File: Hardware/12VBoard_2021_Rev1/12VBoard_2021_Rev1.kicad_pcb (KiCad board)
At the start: 2 copper layers, 125 parts, among them Q1 2N7000, Q2 2N7000, Q3 NTR2101P, Q4 2N7000, Q5 2N7000, Q6 2N7000, Q7 2N7000, U1 LM2576SX-5.0/NOPB, U10 LM5116, U11 INA198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

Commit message: Worked on layout
Low current bucks grouped with their componets
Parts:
- C1, C3, C4, C43, C45, C47, C49, C5, C6: footprint Capacitor_THT:CP_Axial_L20.0mm_D10.0mm_P26.00mm_Horizontal -> Capacitor_THT:CP_Radial_D10.0mm_P5.00mm
- C15, C18, C22, C27, C30, C37, C40: footprint Capacitor_THT:CP_Axial_L20.0mm_D10.0mm_P26.00mm_Horizontal -> Capacitor_THT:CP_Radial_D6.3mm_P2.50mm
- Conn3: footprint MRDT_Connectors:Anderson_2_Horizontal_Stacked -> MRDT_Connectors:Anderson_2_Horizontal_Side_by_Side
- R1: value 1.2k -> 3.3k
- R2: value 1.2k -> 500
- moved TP2 256.2 mm to (192.5, 133.1)
- moved C5 254.8 mm to (197.1, 124.0), turned to 180 degrees
- moved D10 250.7 mm to (191.1, 139.4), turned to 180 degrees
- moved U4 247.7 mm to (142.2, 138.6), turned to 180 degrees
- moved C9 247.3 mm to (204.2, 134.2), turned to 90 degrees
- moved C6 245.1 mm to (168.7, 123.2), turned to 180 degrees
- moved U14 244.3 mm to (109.8, 136.1), turned to 180 degrees
- moved R7 243.6 mm to (163.0, 136.9), turned to 180 degrees
- moved D11 243.4 mm to (163.0, 138.7), turned to 180 degrees
- moved TP8 242.0 mm to (103.6, 130.6)
- moved R6 241.5 mm to (191.1, 137.4), turned to 180 degrees
- moved U6 240.7 mm to (170.4, 139.6), turned to 180 degrees
- moved U1 240.5 mm to (222.2, 140.7), turned to 180 degrees
- moved D6 240.4 mm to (202.1, 130.3)
- moved U5 239.4 mm to (198.9, 140.1), turned to 180 degrees
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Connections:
- D13 pad 1: Net-(D13-Pad1) -> AGNDPGND
- D13 pad 2: /High Current Outputs/Multimedia/Extra/12V10AExtra -> Net-(D13-Pad2)
- D14 pad 1: Net-(D14-Pad1) -> AGNDPGND
- D14 pad 2: /High Current Outputs/Multimedia/Extra/12V10AMultimedia -> Net-(D14-Pad2)
- D16 pad 1: Net-(D16-Pad1) -> AGNDPGND
- D16 pad 2: /High Current Outputs/AuxMount/12V10AAuxMount -> Net-(D16-Pad2)
- D18 pad 1: Net-(D18-Pad1) -> AGNDPGND
- D18 pad 2: /High Current Outputs/Gimbal/12V5AGimbal -> Net-(D18-Pad2)
- D2 pad 1: Net-(D2-Pad1) -> AGNDPGND
- D2 pad 2: /High Current Outputs/PackVoltage -> Net-(D2-Pad2)
- D22 pad 1: Net-(D22-Pad1) -> AGNDPGND
- D22 pad 2: /High Current Outputs/Multimedia/Extra/12V3AMultimediaExtraLogic -> Net-(D22-Pad2)
- D24 pad 1: Net-(D24-Pad1) -> AGNDPGND
- D24 pad 2: /High Current Outputs/Gimbal/12V3AGimbalLogic -> Net-(D24-Pad2)
- D26 pad 1: Net-(D26-Pad1) -> AGNDPGND
- D26 pad 2: /High Current Outputs/AuxMount/12V3AAuxMountLogic -> Net-(D26-Pad2)
- D3 pad 1: Net-(D3-Pad1) -> AGNDPGND
- D3 pad 2: /High Current Outputs/5V -> Net-(D3-Pad2)
- R1 pad 1: Net-(D2-Pad1) -> /High Current Outputs/PackVoltage
- R1 pad 2: AGNDPGND -> Net-(D2-Pad2)
- R2 pad 1: Net-(D3-Pad1) -> /High Current Outputs/5V
- R2 pad 2: AGNDPGND -> Net-(D3-Pad2)
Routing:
- net /High Current Outputs/PackVoltage: track 0.00 -> 6.46 mm
- net Net-(D2-Pad2): track 0.00 -> 4.32 mm
- added copper zone on B.Cu, net AGNDPGND
- added copper zone on F.Cu, net AGNDPGND

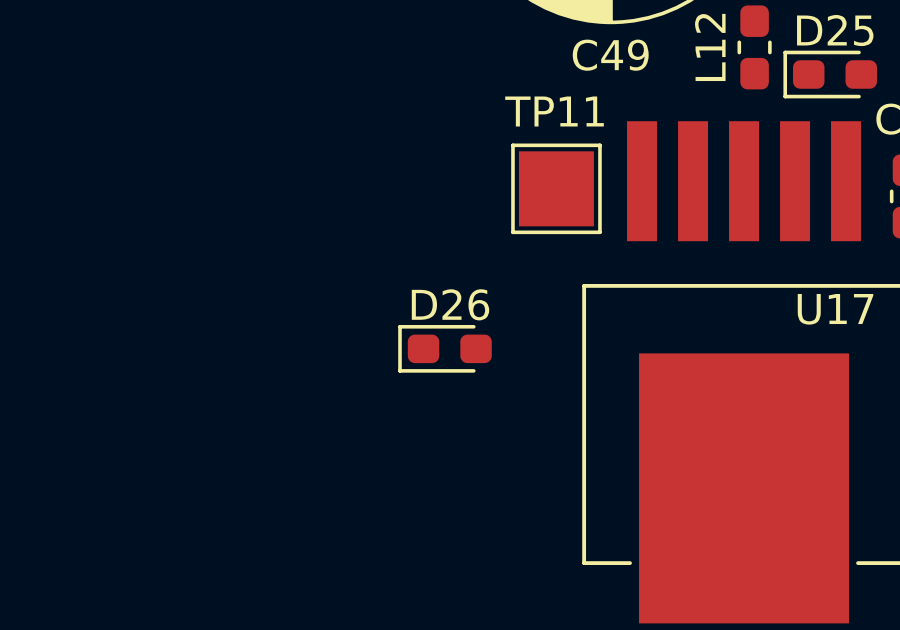
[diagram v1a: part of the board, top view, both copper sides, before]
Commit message: Missing footprints issue found
Library difference between computer caused footprints not to appear on the layout
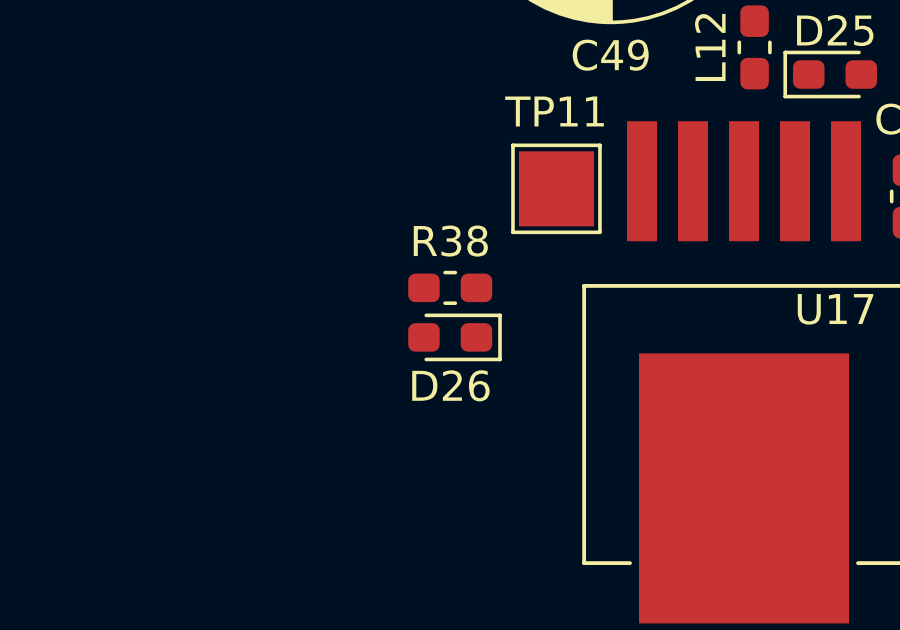
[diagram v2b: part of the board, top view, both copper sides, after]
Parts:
- added R38: 1.2k, Resistor_SMD:R_0603_1608Metric_Pad1.05x0.95mm_HandSolder, F.Cu at (106.4, 62.5)
- moved D26 0.38 mm to (106.4, 64.1), turned to 180 degrees

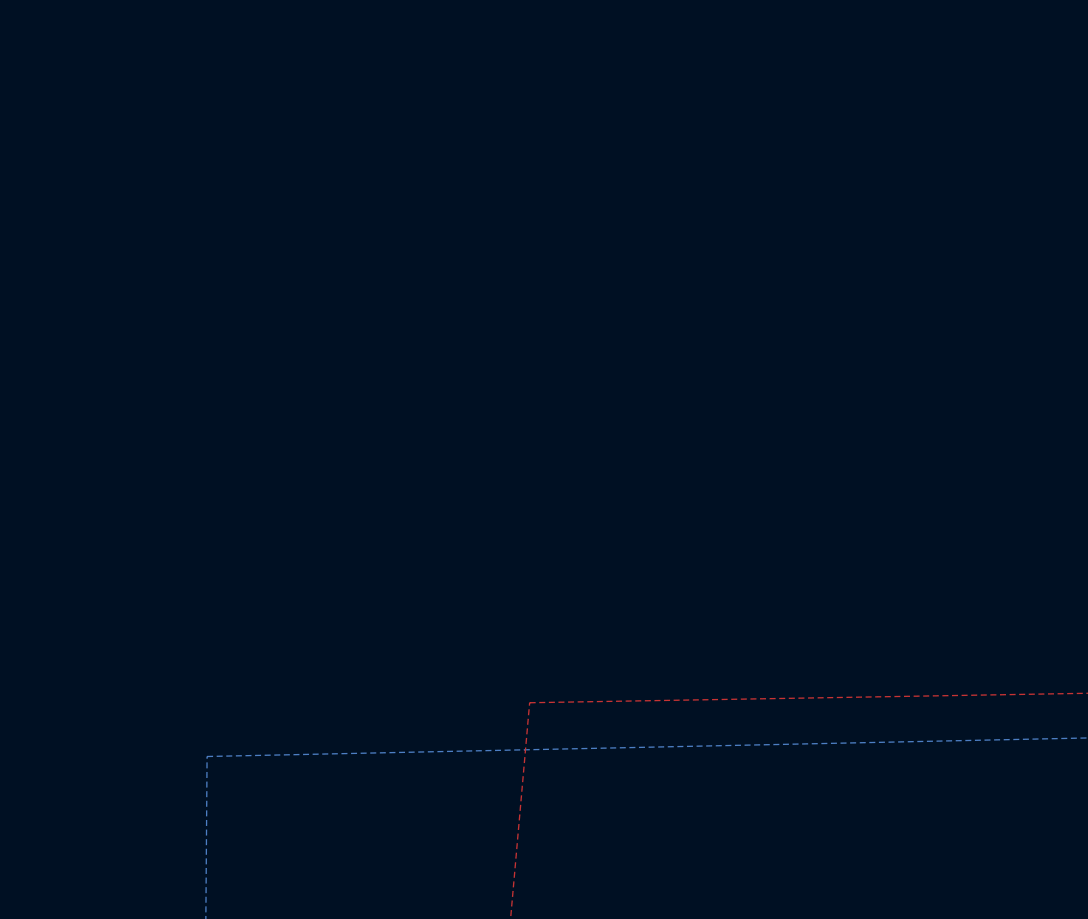
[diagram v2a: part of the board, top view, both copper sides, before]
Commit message: Fixed Resistor and Capasitor footprints
found other issues
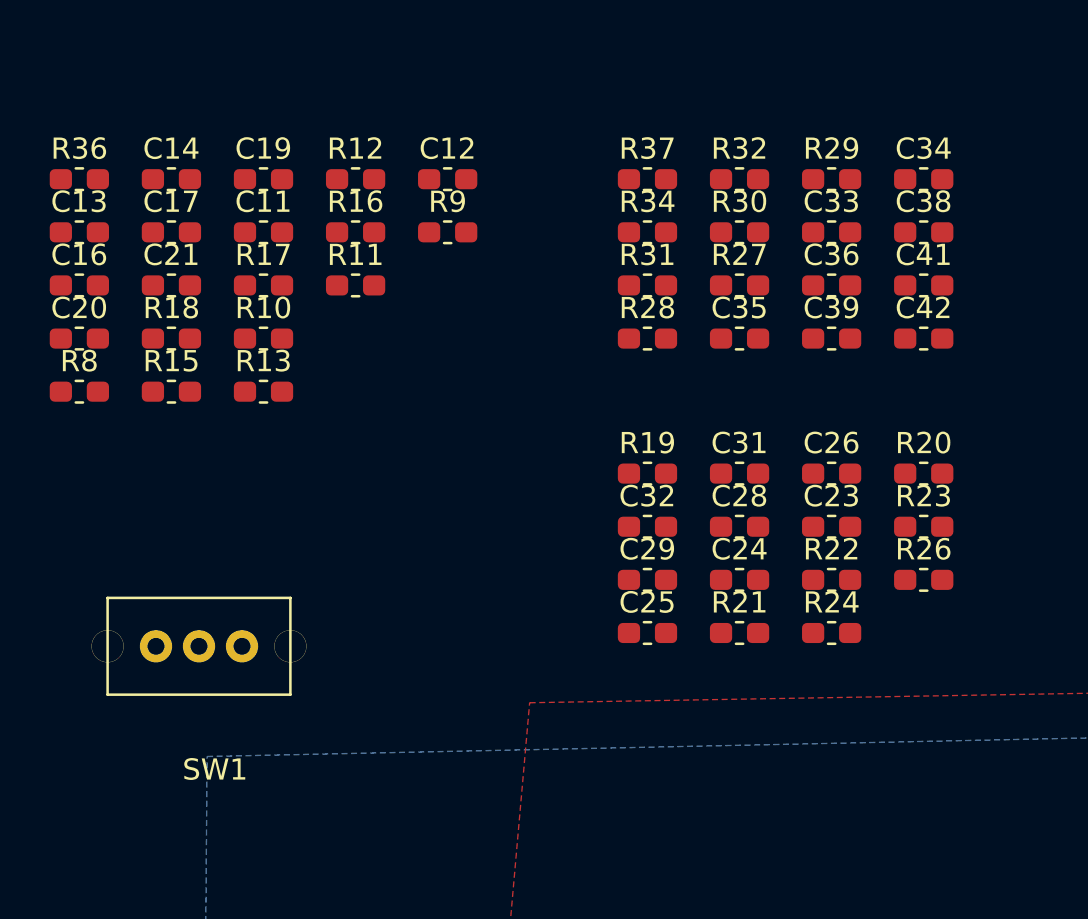
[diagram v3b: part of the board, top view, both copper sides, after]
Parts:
- added C11: 2.2uF, Capacitor_SMD:C_0603_1608Metric_Pad1.05x0.95mm_HandSolder, F.Cu at (40.8, -29.8)
- added C12: 100uF, Capacitor_SMD:C_0603_1608Metric_Pad1.05x0.95mm_HandSolder, F.Cu at (49.5, -32.4)
- added C13: 1uF, Capacitor_SMD:C_0603_1608Metric_Pad1.05x0.95mm_HandSolder, F.Cu at (32.1, -29.8)
- added C14: 100nF, Capacitor_SMD:C_0603_1608Metric_Pad1.05x0.95mm_HandSolder, F.Cu at (36.4, -32.4)
- added C16: 10pF, Capacitor_SMD:C_0603_1608Metric_Pad1.05x0.95mm_HandSolder, F.Cu at (32.1, -27.3)
- added C17: 120pF, Capacitor_SMD:C_0603_1608Metric_Pad1.05x0.95mm_HandSolder, F.Cu at (36.4, -29.8)
- added C19: 470pF, Capacitor_SMD:C_0603_1608Metric_Pad1.05x0.95mm_HandSolder, F.Cu at (40.8, -32.4)
- added C20: 33pF, Capacitor_SMD:C_0603_1608Metric_Pad1.05x0.95mm_HandSolder, F.Cu at (32.1, -24.8)
- added C21: 0.1pF, Capacitor_SMD:C_0603_1608Metric_Pad1.05x0.95mm_HandSolder, F.Cu at (36.4, -27.3)
- added C23: 100nF, Capacitor_SMD:C_0603_1608Metric_Pad1.05x0.95mm_HandSolder, F.Cu at (67.6, -15.9)
- added C24: 2.2uF, Capacitor_SMD:C_0603_1608Metric_Pad1.05x0.95mm_HandSolder, F.Cu at (63.3, -13.4)
- added C25: 1uF, Capacitor_SMD:C_0603_1608Metric_Pad1.05x0.95mm_HandSolder, F.Cu at (58.9, -10.9)
- added C26: 100nF, Capacitor_SMD:C_0603_1608Metric_Pad1.05x0.95mm_HandSolder, F.Cu at (67.6, -18.4)
- added C28: 10pF, Capacitor_SMD:C_0603_1608Metric_Pad1.05x0.95mm_HandSolder, F.Cu at (63.3, -15.9)
- added C29: 120pF, Capacitor_SMD:C_0603_1608Metric_Pad1.05x0.95mm_HandSolder, F.Cu at (58.9, -13.4)
- added C31: 470pF, Capacitor_SMD:C_0603_1608Metric_Pad1.05x0.95mm_HandSolder, F.Cu at (63.3, -18.4)
- added C32: 33nF, Capacitor_SMD:C_0603_1608Metric_Pad1.05x0.95mm_HandSolder, F.Cu at (58.9, -15.9)
- added C33: 100nF, Capacitor_SMD:C_0603_1608Metric_Pad1.05x0.95mm_HandSolder, F.Cu at (67.6, -29.8)
- added C34: 2.2uF, Capacitor_SMD:C_0603_1608Metric_Pad1.05x0.95mm_HandSolder, F.Cu at (72.0, -32.4)
- added C35: 1uF, Capacitor_SMD:C_0603_1608Metric_Pad1.05x0.95mm_HandSolder, F.Cu at (63.3, -24.8)
- added C36: 100nF, Capacitor_SMD:C_0603_1608Metric_Pad1.05x0.95mm_HandSolder, F.Cu at (67.6, -27.3)
- added C38: 10pF, Capacitor_SMD:C_0603_1608Metric_Pad1.05x0.95mm_HandSolder, F.Cu at (72.0, -29.8)
- added C39: 120pF, Capacitor_SMD:C_0603_1608Metric_Pad1.05x0.95mm_HandSolder, F.Cu at (67.6, -24.8)
- added C41: 470pF, Capacitor_SMD:C_0603_1608Metric_Pad1.05x0.95mm_HandSolder, F.Cu at (72.0, -27.3)
- added C42: 33nF, Capacitor_SMD:C_0603_1608Metric_Pad1.05x0.95mm_HandSolder, F.Cu at (72.0, -24.8)
- added R10: 2.26K, Resistor_SMD:R_0603_1608Metric_Pad1.05x0.95mm_HandSolder, F.Cu at (40.8, -24.8)
- added R11: 86.6K, Resistor_SMD:R_0603_1608Metric_Pad1.05x0.95mm_HandSolder, F.Cu at (45.1, -27.3)
- added R12: 9.76, Resistor_SMD:R_0603_1608Metric_Pad1.05x0.95mm_HandSolder, F.Cu at (45.1, -32.4)
- added R13: 261K, Resistor_SMD:R_0603_1608Metric_Pad1.05x0.95mm_HandSolder, F.Cu at (40.8, -22.3)
- added R15: 5.1K, Resistor_SMD:R_0603_1608Metric_Pad1.05x0.95mm_HandSolder, F.Cu at (36.4, -22.3)
- added R16: 0.01, Resistor_SMD:R_0603_1608Metric_Pad1.05x0.95mm_HandSolder, F.Cu at (45.1, -29.8)
- added R17: 1.2k, Resistor_SMD:R_0603_1608Metric_Pad1.05x0.95mm_HandSolder, F.Cu at (40.8, -27.3)
- added R18: 1.2k, Resistor_SMD:R_0603_1608Metric_Pad1.05x0.95mm_HandSolder, F.Cu at (36.4, -24.8)
- added R19: 5m, Resistor_SMD:R_0603_1608Metric_Pad1.05x0.95mm_HandSolder, F.Cu at (58.9, -18.4)
- added R20: 36.5K, Resistor_SMD:R_0603_1608Metric_Pad1.05x0.95mm_HandSolder, F.Cu at (72.0, -18.4)
- added R21: 2.26K, Resistor_SMD:R_0603_1608Metric_Pad1.05x0.95mm_HandSolder, F.Cu at (63.3, -10.9)
- added R22: 86.6K, Resistor_SMD:R_0603_1608Metric_Pad1.05x0.95mm_HandSolder, F.Cu at (67.6, -13.4)
- added R23: 9.76K, Resistor_SMD:R_0603_1608Metric_Pad1.05x0.95mm_HandSolder, F.Cu at (72.0, -15.9)
- added R24: 261K, Resistor_SMD:R_0603_1608Metric_Pad1.05x0.95mm_HandSolder, F.Cu at (67.6, -10.9)
- added R26: 1.2k, Resistor_SMD:R_0603_1608Metric_Pad1.05x0.95mm_HandSolder, F.Cu at (72.0, -13.4)
- added R27: 5m, Resistor_SMD:R_0603_1608Metric_Pad1.05x0.95mm_HandSolder, F.Cu at (63.3, -27.3)
- added R28: 36.5K, Resistor_SMD:R_0603_1608Metric_Pad1.05x0.95mm_HandSolder, F.Cu at (58.9, -24.8)
- added R29: 2.26K, Resistor_SMD:R_0603_1608Metric_Pad1.05x0.95mm_HandSolder, F.Cu at (67.6, -32.4)
- added R30: 86.6K, Resistor_SMD:R_0603_1608Metric_Pad1.05x0.95mm_HandSolder, F.Cu at (63.3, -29.8)
- added R31: 9.76k, Resistor_SMD:R_0603_1608Metric_Pad1.05x0.95mm_HandSolder, F.Cu at (58.9, -27.3)
- added R32: 261K, Resistor_SMD:R_0603_1608Metric_Pad1.05x0.95mm_HandSolder, F.Cu at (63.3, -32.4)
- added R34: 1.2k, Resistor_SMD:R_0603_1608Metric_Pad1.05x0.95mm_HandSolder, F.Cu at (58.9, -29.8)
- added R36: 1.2k, Resistor_SMD:R_0603_1608Metric_Pad1.05x0.95mm_HandSolder, F.Cu at (32.1, -32.4)
- added R37: 1.2k, Resistor_SMD:R_0603_1608Metric_Pad1.05x0.95mm_HandSolder, F.Cu at (58.9, -32.4)
- added R8: 5m, Resistor_SMD:R_0603_1608Metric_Pad1.05x0.95mm_HandSolder, F.Cu at (32.1, -22.3)
- added R9: 36.5K, Resistor_SMD:R_0603_1608Metric_Pad1.05x0.95mm_HandSolder, F.Cu at (49.5, -29.8)
- added SW1: SW_SPDT, MRDT_12VoltBoard:Switch_OS102011MA1QN1, F.Cu at (38.5, -4.95)
